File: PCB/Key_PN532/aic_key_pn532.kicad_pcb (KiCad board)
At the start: 2 copper layers, 50 x 50 mm, 33 parts, among them J1 PN532, SW1 SKRR_4pin, SW10 SKRR_4pin, SW11 SKRR_4pin, SW12 SKRR_4pin, SW2 SKRR_4pin, SW3 SKRR_4pin, SW4 SKRR_4pin, SW5 SKRR_4pin, SW6 SKRR_4pin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

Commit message: PCB v1.1, pad optimization
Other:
- board text added: "AIC Key v1.1"
- board text removed: "AIC Key v1.0"

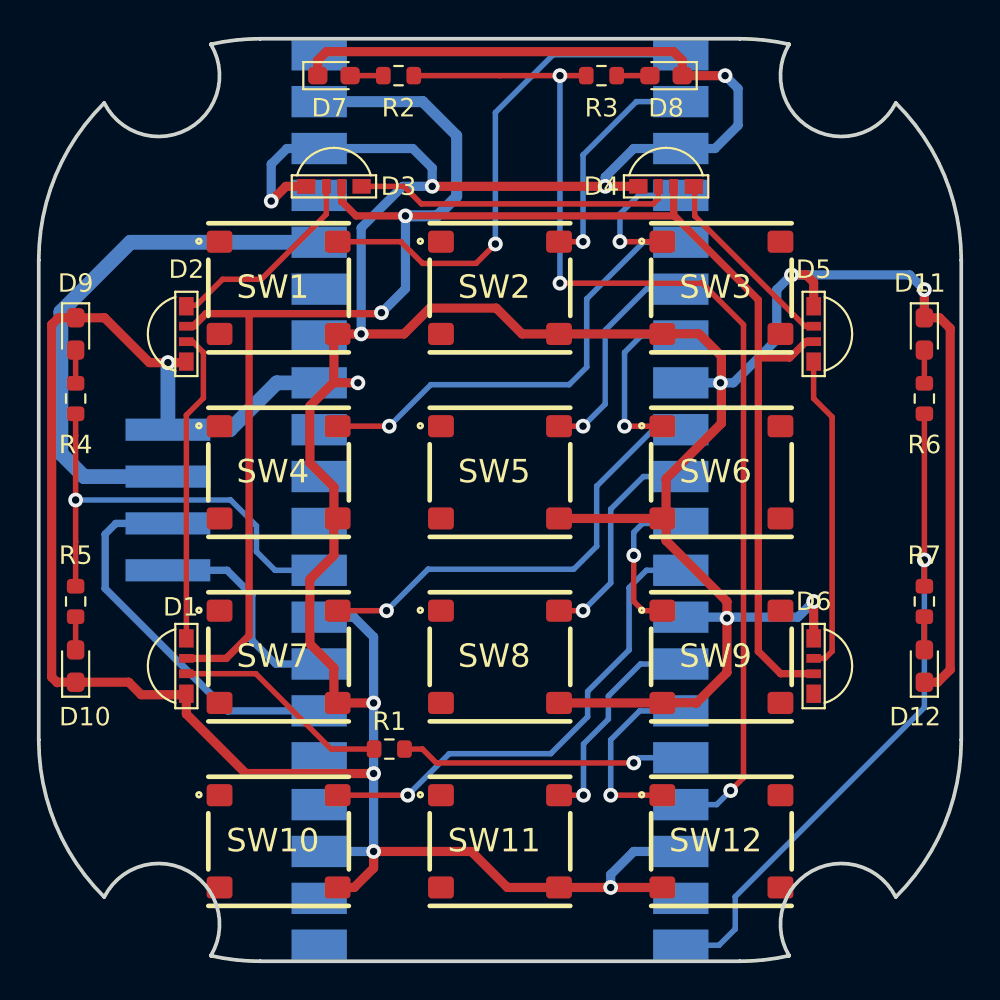
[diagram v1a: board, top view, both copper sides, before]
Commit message: WS2812C-2020 option for AIC Key PN532
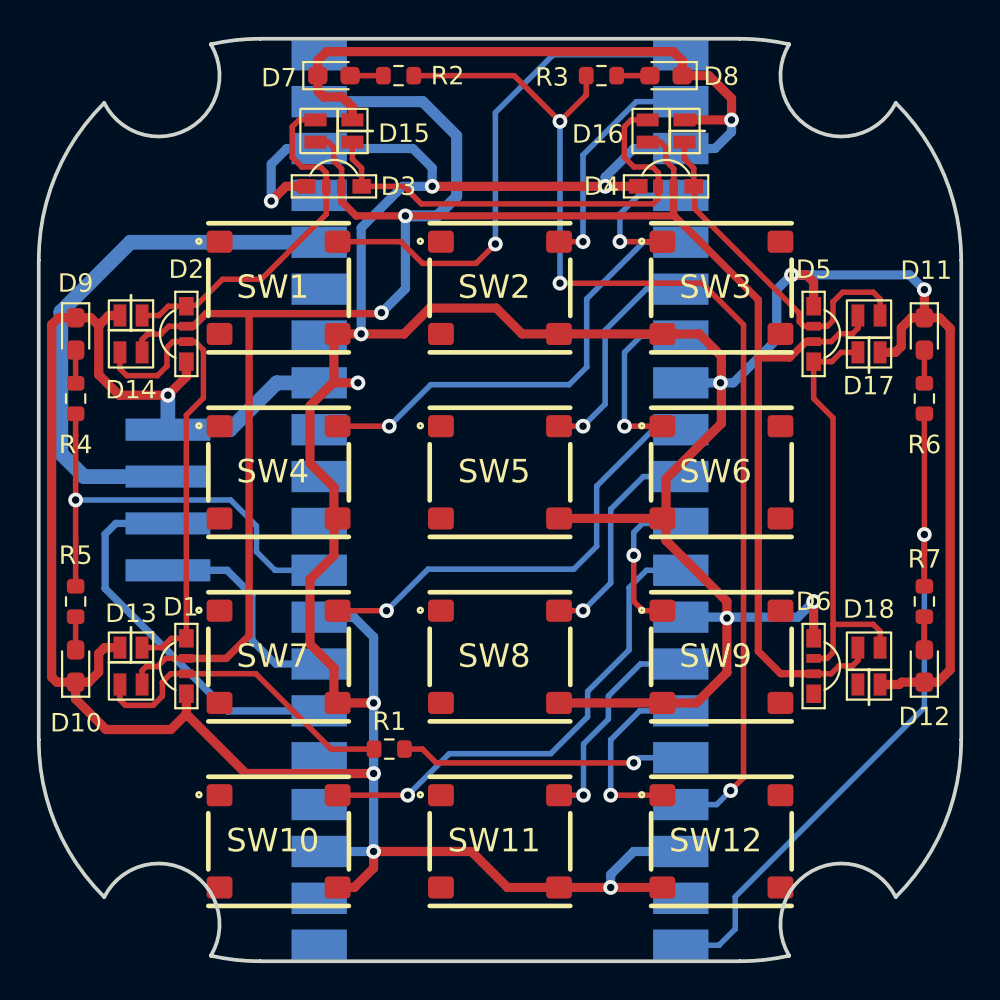
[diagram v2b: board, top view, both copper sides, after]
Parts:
- added D13: WS2812B_Unified, aic_pico:WS2812C-2020, F.Cu at (115.3, 122.4)
- added D14: WS2812B_Unified, aic_pico:WS2812C-2020, F.Cu at (115.3, 104.4)
- added D15: WS2812B_Unified, aic_pico:WS2812C-2020, F.Cu at (126.3, 93.4)
- added D16: WS2812B_Unified, aic_pico:WS2812C-2020, F.Cu at (144.3, 93.4)
- added D17: WS2812B_Unified, aic_pico:WS2812C-2020, F.Cu at (155.3, 104.4)
- added D18: WS2812B_Unified, aic_pico:WS2812C-2020, F.Cu at (155.3, 122.4)
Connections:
- net Net-(D1-In) renamed /L1
- net Net-(D1-Out) renamed /L2
- net Net-(D2-Out) renamed /L3
- net Net-(D3-Out) renamed /L4
- net Net-(D4-Out) renamed /L5
- net Net-(D5-Out) renamed /L6
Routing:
- net +5V: track 105.8 -> 126.2 mm
- net GND: track 315.2 -> 335.5 mm
- net /L2: track 17.0 -> 25.7 mm
- net /L5: track 10.5 -> 19.2 mm
- net /L4: track 17.2 -> 25.8 mm
- net /L3: track 11.1 -> 19.7 mm
- net /L6: track 17.2 -> 23.4 mm
- net /L1: track 11.9 -> 17.6 mm
- net Net-(U1-GPIO15): track 36.9 -> 38.3 mm
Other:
- board text added: "AIC Key v1.2"
- board text removed: "AIC Key v1.1"

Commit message: Optimize LED 1204 footprint
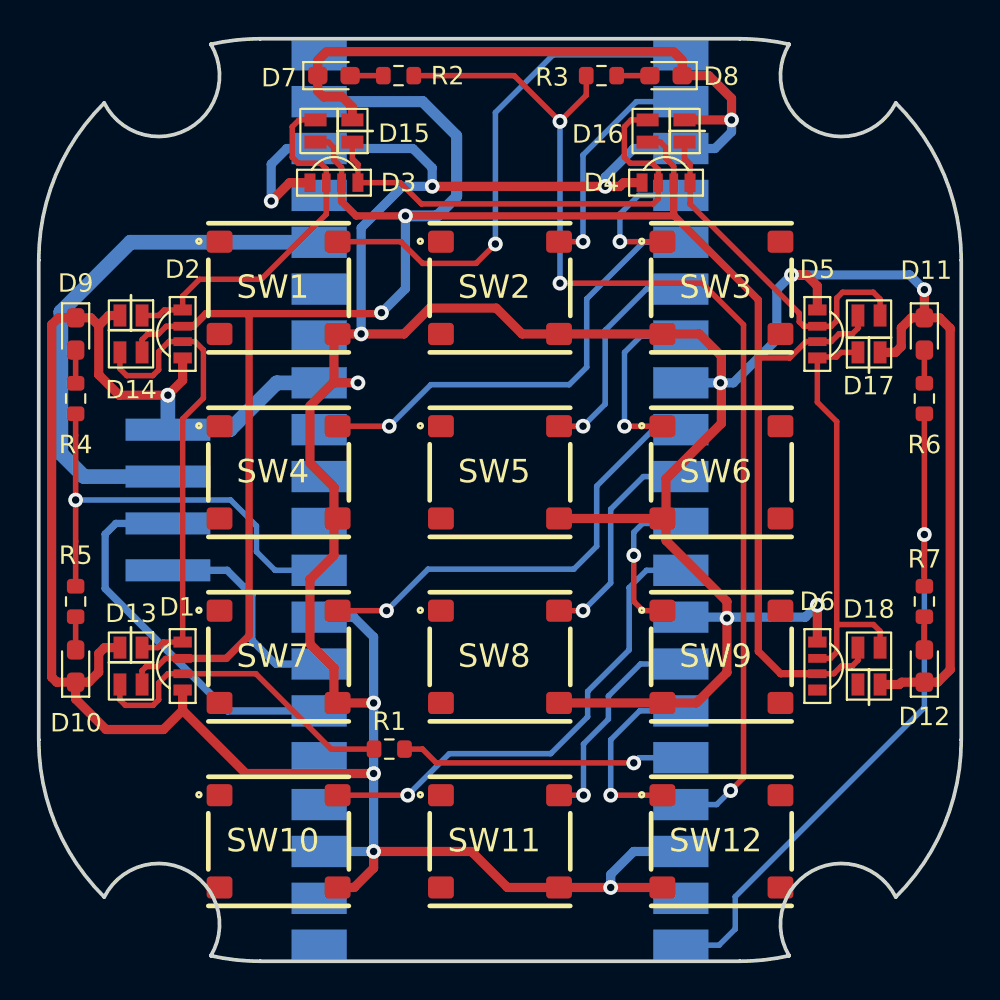
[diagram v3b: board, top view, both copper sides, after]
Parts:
- moved D5 0.20 mm to (152.5, 104.4)
- moved D6 0.20 mm to (152.5, 122.4)
- moved D3 0.20 mm to (126.3, 96.2)
- moved D4 0.20 mm to (144.3, 96.2)
- moved D1 0.20 mm to (118.1, 122.4)
- moved D2 0.20 mm to (118.1, 104.4)
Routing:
- net GND: track 335.5 -> 337.0 mm
- net /L3: track 19.7 -> 20.3 mm
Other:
- board text added: "AIC Key v1.3"
- board text removed: "AIC Key v1.2"
